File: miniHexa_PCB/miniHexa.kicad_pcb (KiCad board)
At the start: 4 copper layers, 94 x 65.9 mm, 78 parts, among them J2 12v DC, SW1 SW_Push, U1 STM32F401RETx, U3 RT8289GSP, U4 BQ25886RGE, U5 PCA9685BS, U6 AMS1117-3.3, Y2 25mhz

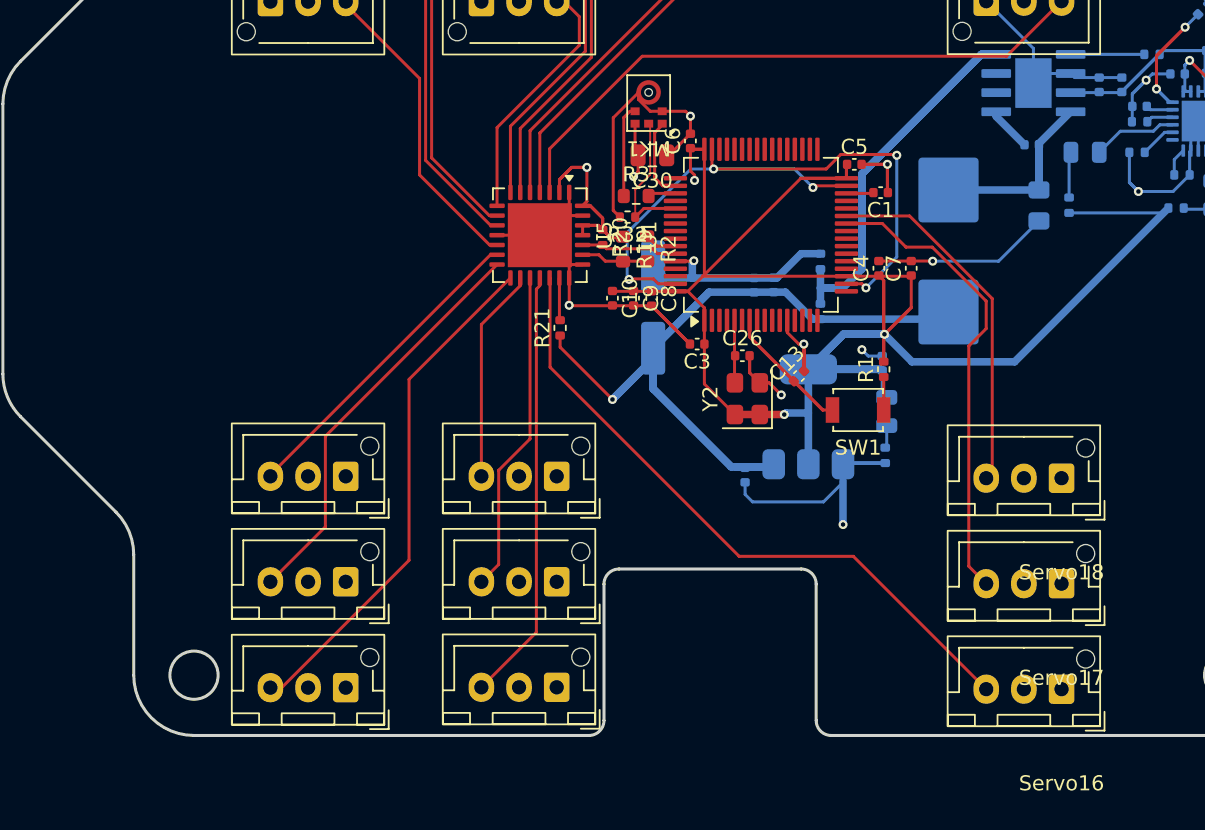
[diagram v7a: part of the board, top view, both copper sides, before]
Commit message: added water marks
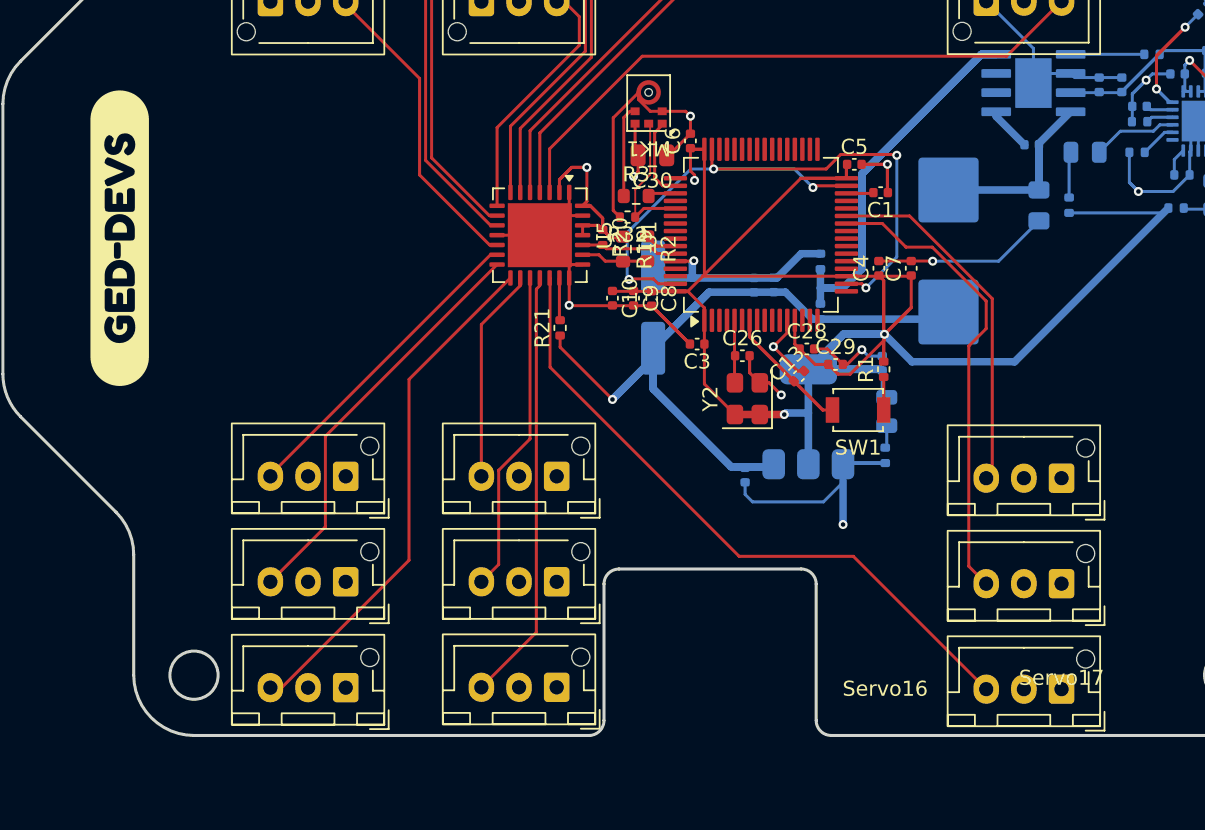
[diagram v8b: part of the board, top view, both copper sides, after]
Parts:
- added C28: 10nF, Capacitor_SMD:C_0402_1005Metric, F.Cu at (170.1, 92.0)
- added C29: 1uF, Capacitor_SMD:C_0402_1005Metric, F.Cu at (172.0, 93.1)
- added kibuzzard-6A883BEF: G***, kibuzzard-6A883BEF, F.Cu at (124.5, 84.7)
- added kibuzzard-6A883C46: G***, kibuzzard-6A883C46, B.Cu at (133.6, 86.1)
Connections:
- net Net-(U4-VBUS) renamed /Power_handler/12V
- U1 pad 13: unconnected-(U1-VREF+-Pad13) -> +3.3V
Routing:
- net +3.3V: track 148.0 -> 157.7 mm
- net GND: track 215.5 -> 218.6 mm
